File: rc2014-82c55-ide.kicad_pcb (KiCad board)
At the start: 2 copper layers, 100 x 50 mm, 23 parts, among them J1 CONN_01X02, J2 IDE connector, J3 IDE connector, J5 CONN_01X03, P1 RC2014 BUS, SW1 SW_DIP_x06, U1 82C55A_PLCC, U2 74HCT688, U3 74HCT04

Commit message: r2 as sent for manufacturing
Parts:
- D1: footprint LEDs:LED_D1.8mm_W3.3mm_H2.4mm -> LEDs:LED_D3.0mm
- J1: value CONN_01X02 -> External power
- J5: value CONN_01X03 -> IDE power from bus; footprint Pin_Headers:Pin_Header_Straight_1x03_Pitch2.54mm -> Pin_Headers:Pin_Header_Straight_1x02_Pitch2.54mm
- moved J1 1.91 mm to (151.1, 139.1)
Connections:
- J1 pad 1: /EXT_VCC -> /IDE_VCC
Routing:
- net GND: track 224.8 -> 239.9 mm
- net /EXT_VCC: track 10.7 -> 0.00 mm
- net VCC: track 247.4 -> 253.9 mm
- net /IDE_VCC: track 31.4 -> 35.9 mm
- net //WR: track 33.4 -> 30.5 mm
- net //PIO_CS: track 86.8 -> 88.9 mm
- net //IORQ: track 61.6 -> 63.4 mm
- net //RD: track 32.7 -> 33.9 mm
- net //DIOR: track 35.5 -> 36.3 mm
- net //DIOW: track 37.4 -> 37.8 mm, vias 2 -> 3
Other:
- board text added: "+5v"
- board text added: "04 08 10 20 40 80"
- board text added: "1-2 2-3 PC0 PC4 PC4 PC0 PC1 PC6 PC6 PC1"
- board text added: "Active"
- board text added: "External Power"
- board text added: "JP1: DA0 JP2: DCS1 JP3: DA1 JP4: DIOR"
- board text added: "RC2014 IDE adapter"
- board text added: "Rev 2"
- board text added: "Use bus power"
- board text removed: "1-2 2-3 JP1: DA0 PC0 PC4 JP2: DCS1 PC4 PC0 JP3: DA1 PC1 PC6 JP4: DIOR PC6 PC1"
- board text removed: "5v"
- board text removed: "Activity"
- board text removed: "Bus"
- board text removed: "Ext"
- board text removed: "RC2014 IDE Adapter"
- board text removed: "Rev 1"
- board text removed: "VCC"

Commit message: Migration to KiCAD 6 WIP
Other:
- net class Default removed
- net class Power removed

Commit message: aisler drc updates
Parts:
- C2: value 0.1uF -> C_Small
- J1: value External power -> Conn_01x02
- J2: value IDE connector -> Conn_02x20_Odd_Even
- J3: value IDE connector -> Conn_02x22_Odd_Even
- J5: value IDE power from bus -> Conn_01x02
- JP1, JP2, JP3, JP4: value Jumper_Dual -> Jumper_3_Bridged12
- P1: value RC2014 BUS -> Conn_01x39
- RN1: value 10K -> R_Network07; footprint Resistors_THT:R_Array_SIP8 -> Resistor_THT:R_Array_SIP8
- U1: footprint Sockets:PLCC44 -> Package_LCC:PLCC-44_THT-Socket
- moved U1 6.48 mm to (141.0, 147.3), turned to -90 degrees
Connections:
- net //ACT renamed //ACT
- net //DCS0 renamed //DCS0
- net //DCS1 renamed //DCS1
- net //DIOR renamed //DIOR
- net //DIOW renamed //DIOW
- net //DRESET renamed //DRESET
- net //IORQ renamed //IORQ
- net //M1 renamed //M1
- net //PIO_CS renamed //PIO_CS
- net //RD renamed //RD
- net //RESET renamed //RESET
- net //WR renamed //WR
- J2 pad 20: (no net) -> unconnected-(J2-Pad20)
- J2 pad 27: (no net) -> unconnected-(J2-Pad27)
- J2 pad 31: (no net) -> unconnected-(J2-Pad31)
- J2 pad 32: (no net) -> unconnected-(J2-Pad32)
- J2 pad 34: (no net) -> unconnected-(J2-Pad34)
- J3 pad 20: (no net) -> unconnected-(J3-Pad20)
- J3 pad 27: (no net) -> unconnected-(J3-Pad27)
- J3 pad 31: (no net) -> unconnected-(J3-Pad31)
- J3 pad 32: (no net) -> unconnected-(J3-Pad32)
- J3 pad 34: (no net) -> unconnected-(J3-Pad34)
- P1 pad 1: (no net) -> unconnected-(P1-Pad1)
- P1 pad 2: (no net) -> unconnected-(P1-Pad2)
- P1 pad 21: (no net) -> unconnected-(P1-Pad21)
- P1 pad 22: (no net) -> unconnected-(P1-Pad22)
- P1 pad 23: (no net) -> unconnected-(P1-Pad23)
- P1 pad 3: (no net) -> unconnected-(P1-Pad3)
- P1 pad 35: (no net) -> unconnected-(P1-Pad35)
- P1 pad 36: (no net) -> unconnected-(P1-Pad36)
- P1 pad 37: (no net) -> unconnected-(P1-Pad37)
- P1 pad 38: (no net) -> unconnected-(P1-Pad38)
- P1 pad 39: (no net) -> unconnected-(P1-Pad39)
- P1 pad 4: (no net) -> unconnected-(P1-Pad4)
- P1 pad 5: (no net) -> unconnected-(P1-Pad5)
- P1 pad 6: (no net) -> unconnected-(P1-Pad6)
- P1 pad 7: (no net) -> unconnected-(P1-Pad7)
- P1 pad 8: (no net) -> unconnected-(P1-Pad8)
- U1 pad 1: (no net) -> unconnected-(U1-Pad1)
- U1 pad 12: (no net) -> unconnected-(U1-Pad12)
- U1 pad 23: (no net) -> unconnected-(U1-Pad23)
- U1 pad 34: (no net) -> unconnected-(U1-Pad34)
- U3 pad 14: VCC -> (no net)
- U3 pad 7: GND -> (no net)
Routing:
- net GND: track 239.9 -> 242.3 mm
- net /D7: track 25.8 -> 27.5 mm
- net //M1: track 38.4 -> 39.8 mm
- net //RD: track 33.9 -> 35.0 mm
- net /PB7: track 58.3 -> 59.3 mm
- net Net-(RN1-Pad5): track 37.0 -> 38.1 mm
- net Net-(RN1-Pad6): track 21.7 -> 22.7 mm
- net /PA3: track 57.8 -> 58.8 mm
- net Net-(RN1-Pad8): track 38.1 -> 39.1 mm
- net /PB2: track 80.7 -> 81.7 mm
- net /PC3: track 40.2 -> 41.0 mm
- net /PA2: track 52.2 -> 53.0 mm
- net /A5: track 10.8 -> 11.5 mm
- net /A1: track 57.0 -> 57.6 mm
- net //DIOW: track 37.8 -> 37.2 mm, vias 3 -> 2
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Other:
- board text added: "2017-2022 Ed Brindley"
- board text removed: "2017 Ed Brindley"

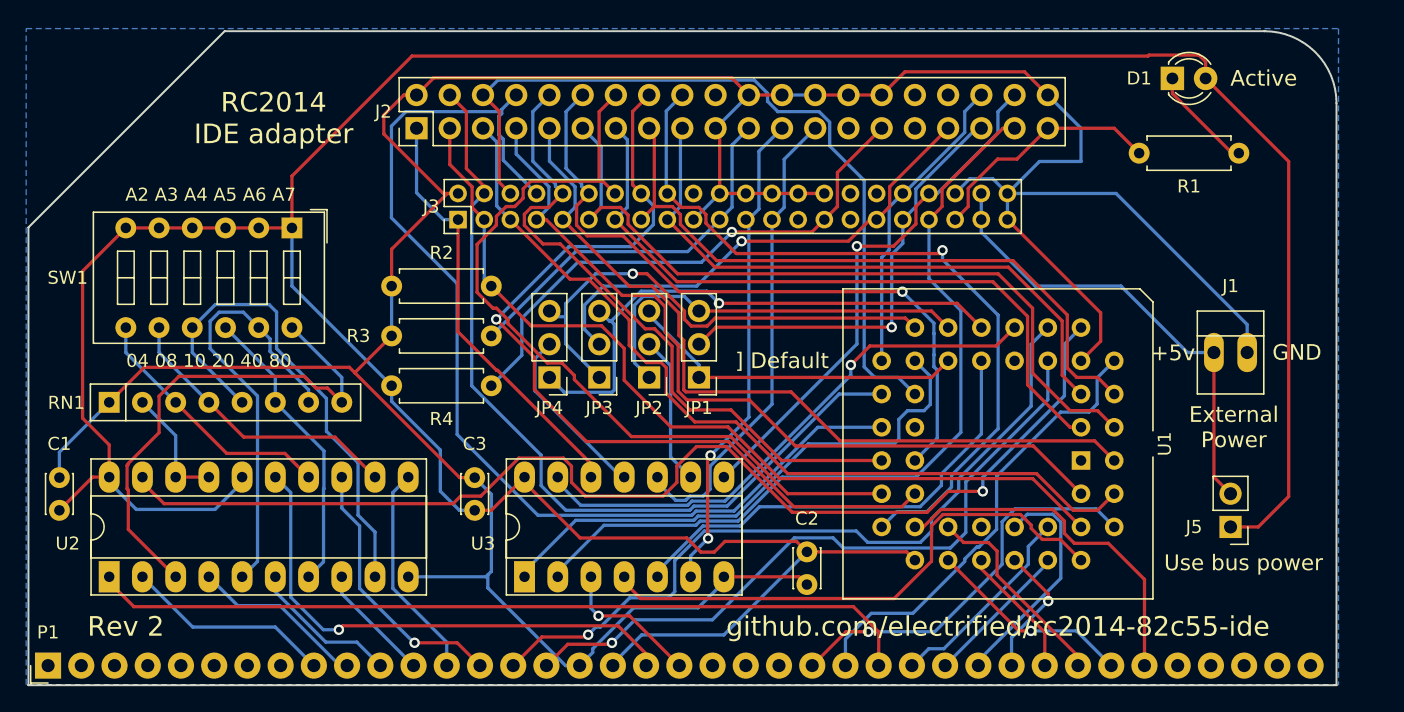
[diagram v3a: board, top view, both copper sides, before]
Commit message: Don't update to asler DRC rules
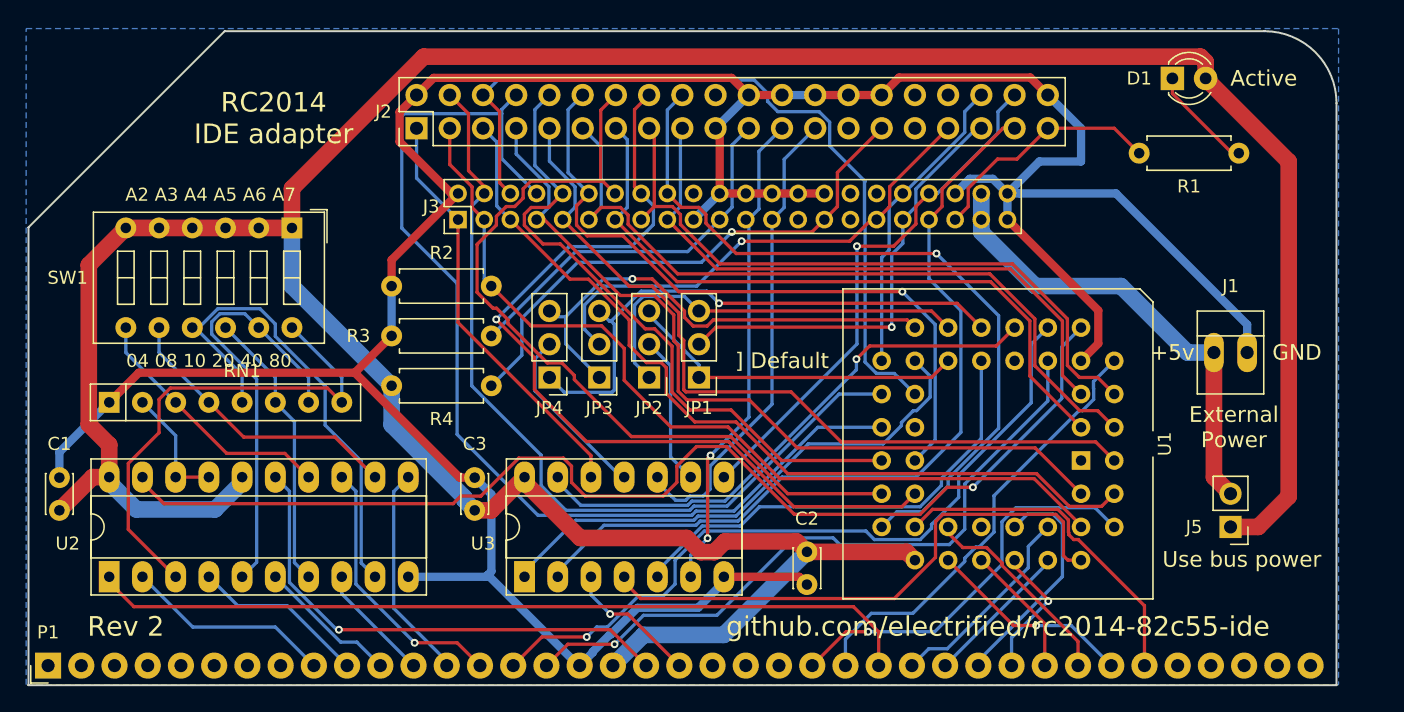
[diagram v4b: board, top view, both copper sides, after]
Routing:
- net GND: track 242.3 -> 239.1 mm
- net VCC: track 254.3 -> 252.5 mm
- net Net-(RN1-Pad5): track 38.1 -> 36.6 mm
- net /RESET: track 41.3 -> 42.7 mm
- net //M1: track 39.8 -> 38.4 mm
- net /PC1: track 37.7 -> 36.6 mm
- net /PC3: track 41.0 -> 39.9 mm
- net /D7: track 27.5 -> 26.4 mm
- net //RD: track 35.0 -> 34.0 mm
- net Net-(RN1-Pad6): track 22.7 -> 21.7 mm
- net Net-(RN1-Pad8): track 39.1 -> 38.1 mm
- net /PB2: track 81.7 -> 80.7 mm
- net /PA3: track 58.8 -> 58.0 mm
- net /PB7: track 59.3 -> 58.6 mm
- net /D5: track 15.1 -> 15.8 mm
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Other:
- board text added: "2017 Ed Brindley"
- board text removed: "2017-2022 Ed Brindley"

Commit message: Further kicad 6 migration
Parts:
- C1, C2, C3: footprint Capacitors_THT:C_Disc_D3.0mm_W2.0mm_P2.50mm -> Capacitor_THT:C_Disc_D3.0mm_W2.0mm_P2.50mm
- D1: footprint LEDs:LED_D3.0mm -> LED_THT:LED_D3.0mm
- J1: footprint Connectors:PINHEAD1-2 -> Connector_PinHeader_2.54mm:PinHeader_1x02_P2.54mm_Vertical
- J2: footprint Pin_Headers:Pin_Header_Straight_2x20_Pitch2.54mm -> Connector_PinHeader_2.54mm:PinHeader_2x20_P2.54mm_Vertical
- J3: footprint Pin_Headers:Pin_Header_Straight_2x22_Pitch2.00mm -> Connector_PinHeader_2.00mm:PinHeader_2x22_P2.00mm_Vertical
- J5: footprint Pin_Headers:Pin_Header_Straight_1x02_Pitch2.54mm -> Connector_PinHeader_2.54mm:PinHeader_1x02_P2.54mm_Vertical
- JP1, JP2, JP3, JP4: footprint Pin_Headers:Pin_Header_Straight_1x03_Pitch2.54mm -> Connector_PinHeader_2.54mm:PinHeader_1x03_P2.54mm_Vertical
- R1, R2, R3, R4: footprint Resistors_THT:R_Axial_DIN0207_L6.3mm_D2.5mm_P7.62mm_Horizontal -> Resistor_THT:R_Axial_DIN0207_L6.3mm_D2.5mm_P7.62mm_Horizontal
- SW1: footprint Buttons_Switches_THT:SW_DIP_x6_W7.62mm_Slide -> Button_Switch_THT:SW_DIP_SPSTx06_Slide_9.78x17.42mm_W7.62mm_P2.54mm
- U2: footprint Housings_DIP:DIP-20_W7.62mm_Socket_LongPads -> Package_DIP:DIP-20_W7.62mm_Socket_LongPads
- U3: footprint Housings_DIP:DIP-14_W7.62mm_Socket_LongPads -> Package_DIP:DIP-14_W7.62mm_Socket_LongPads
- moved J1 0.76 mm to (151.9, 139.1), turned to 90 degrees
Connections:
- net //ACT renamed /~{ACT}
- net //DCS0 renamed /~{DCS0}
- net //DCS1 renamed /~{DCS1}
- net //DIOR renamed /~{DIOR}
- net //DIOW renamed /~{DIOW}
- net //DRESET renamed /~{DRESET}
- net //IORQ renamed /~{IORQ}
- net //M1 renamed /~{M1}
- net //PIO_CS renamed /~{PIO_CS}
- net //RD renamed /~{RD}
- net //RESET renamed /~{RESET}
- net //WR renamed /~{WR}
- U3 pad 14: (no net) -> VCC
- U3 pad 7: (no net) -> GND
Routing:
- net Net-(RN1-Pad5): track 36.6 -> 37.2 mm
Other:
- board text added: "2017-2022 Ed Brindley"
- board text added: "Rev 3-pre"
- board text removed: "2017 Ed Brindley"
- board text removed: "Rev 2"

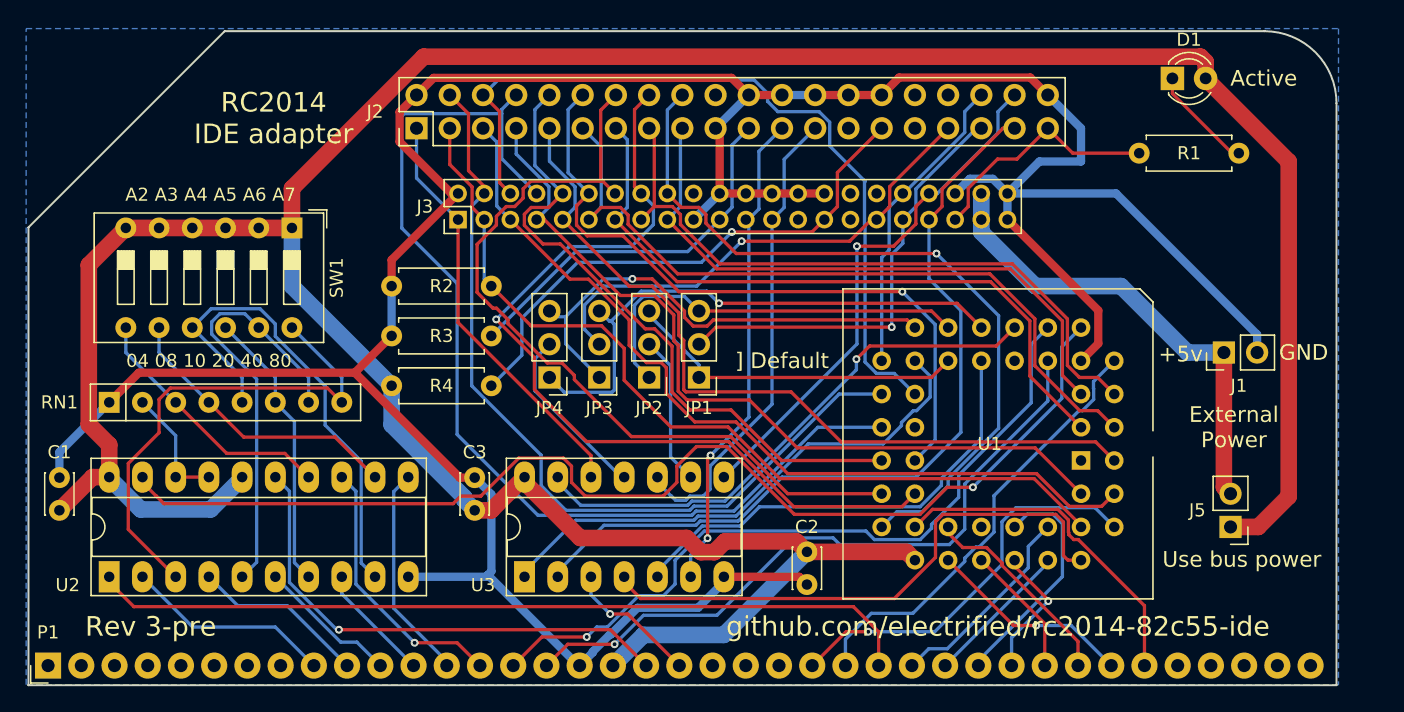
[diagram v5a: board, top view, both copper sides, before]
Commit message: Remove unused footprints
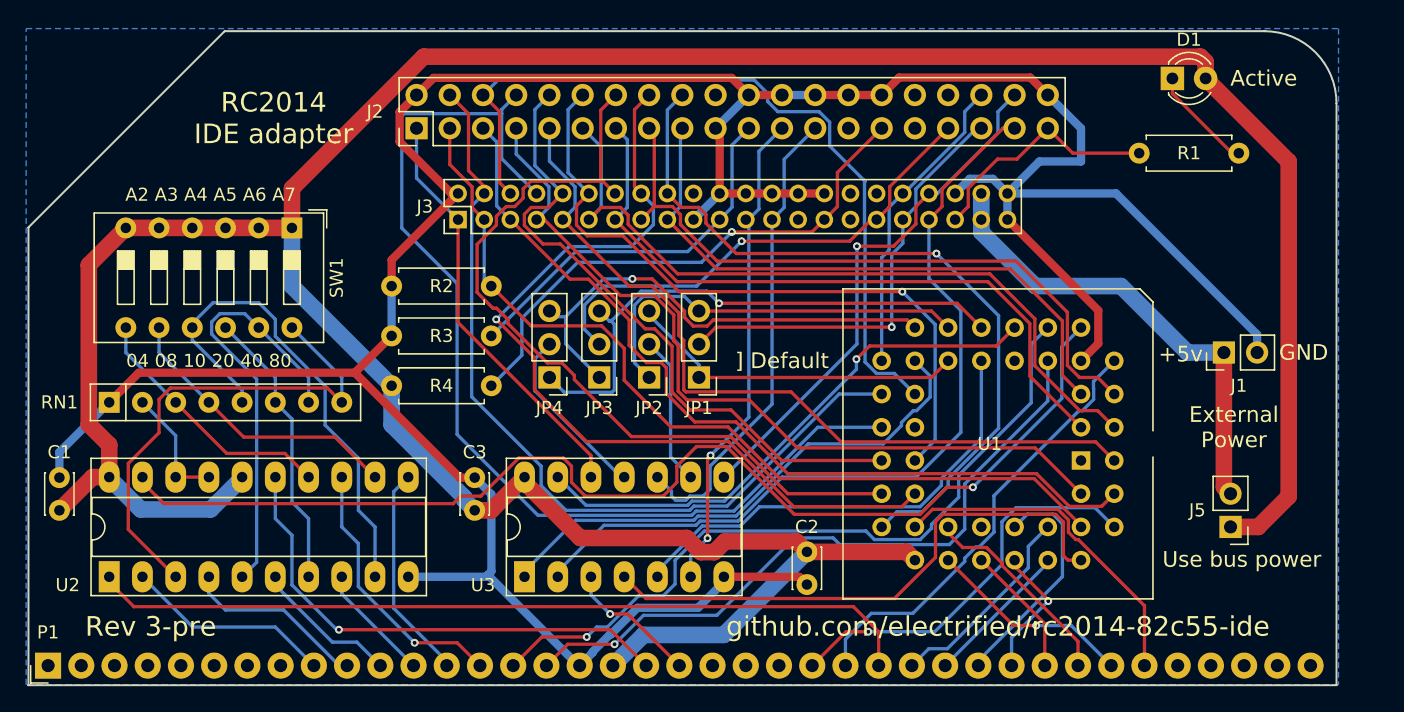
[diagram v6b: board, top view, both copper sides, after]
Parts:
- REF***: footprint Symbols:OSHW-Logo2_14.6x12mm_SilkScreen -> Symbol:OSHW-Logo2_14.6x12mm_SilkScreen
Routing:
- net /PA1: track 50.6 -> 51.5 mm
- net Net-(RN1-Pad5): track 37.2 -> 38.0 mm
- net /A6: track 13.4 -> 14.1 mm
- net Net-(D1-Pad1): track 7.60 -> 8.12 mm
